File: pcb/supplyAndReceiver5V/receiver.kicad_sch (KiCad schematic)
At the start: 7 parts, among them J1 Conn_01x05_Socket, J1 WAGO 2061-602, J2 har-flexicon 2,54 MSH-4, J4 Kyocera-009176002001906, U2 ISL3280ExHZ

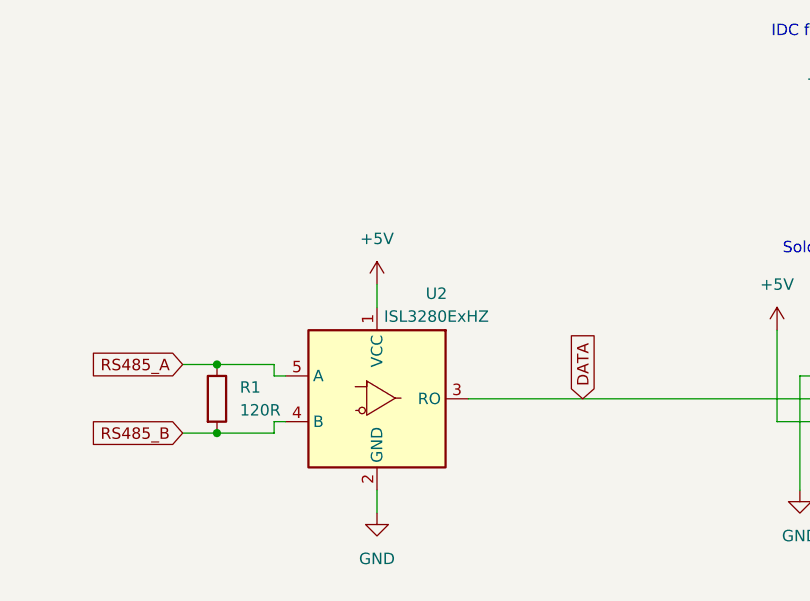
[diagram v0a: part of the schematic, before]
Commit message: Use ISL3280E
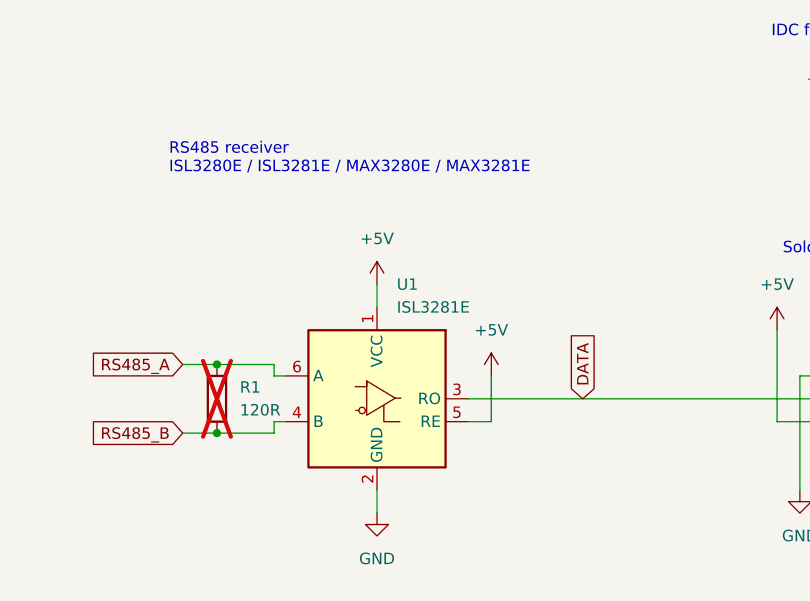
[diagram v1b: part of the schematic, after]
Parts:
- removed U2: ISL3280ExHZ, local:ISL3280E, symbol Interface_UART:ISL3280ExHZ
- added U1: ISL3281E, local:ISL3281E, symbol Interface_UART:ISL3281ExHZ
- R1: now not fitted
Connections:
- net +5V: now also U1.1 (VCC), U1.5 (RE)
- net DATA: now also U1.3 (RO)
- net GND: now also U1.2 (GND)
- net RS485_A: now also U1.6 (A)
- net RS485_B: now also U1.4 (B)
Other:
- note added: "RS485 receiver ISL3280E / ISL3281E / MAX3280E / MAX3281E"
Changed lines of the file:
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@@
+	(wire
+		(pts
+			(xy 135.89 95.25) (xy 135.89 90.17)
+		)
+		(stroke
+			(width 0)
+			(type default)
+		)
+	)
 	(wire
 		(pts
@@
 		(pts
 			(xy 46.99 118.745) (xy 61.595 118.745)
+		)
+		(stroke
+			(width 0)
+			(type default)
+		)
+	)
+	(wire
+		(pts
+			(xy 133.35 95.25) (xy 135.89 95.25)
 		)
 		(stroke
@@
 		)
 	)
+	(text "RS485 receiver\nISL3280E / ISL3281E / MAX3280E / MAX3281E"
+		(exclude_from_sim no)
+		(at 100.076 67.818 0)
+		(effects
+			(font
+				(size 1.27 1.27)
+			)
+			(justify left bottom)
+		)
+	)
 	(text "Solder to LED strip"
 		(exclude_from_sim no)
@@
 	)
 	(symbol
-		(lib_id "Interface_UART:ISL3280ExHZ")
-		(at 123.19 92.71 0)
-		(unit 1)
-		(exclude_from_sim no)
-		(in_bom yes)
-		(on_board yes)
-		(dnp no)
-		(property "Reference" "U2"
-			(at 129.794 81.026 0)
-			(effects
-				(font
-					(size 1.27 1.27)
-				)
-			)
-		)
-		(property "Value" "ISL3280ExHZ"
-			(at 129.794 83.566 0)
-			(effects
-				(font
-					(size 1.27 1.27)
-				)
-			)
-		)
-		(property "Footprint" "local:ISL3280E"
-			(at 125.73 78.74 0)
-			(effects
-				(font
-					(size 1.27 1.27)
-				)
-				(justify left)
-				(hide yes)
-			)
-		)
-		(property "Datasheet" "https://www.renesas.com/us/en/www/doc/datasheet/isl3280e-81e-82e-83e-84e-85e.pdf"
-			(at 100.33 74.93 0)
-			(effects
-				(font
-					(size 1.27 1.27)
-				)
-				(hide yes)
-			)
-		)
-		(property "Description" "RS485, RS422, 20Mbps Transceiver, 3.0V to 5.5V, SOT-23-5"
-			(at 123.19 92.71 0)
-			(effects
-				(font
-					(size 1.27 1.27)
-				)
-				(hide yes)
-			)
-		)
-		(pin "4"
-		)
-		(pin "1"
-		)
-		(pin "2"
-		)
-		(pin "3"
-		)
-		(pin "5"
-		)
-		(instances
-			(project "receiver"
-				(path "/b9a04c3c-65eb-4e1c-b3ab-7b6c9af3c411"
-					(reference "U2")
-					(unit 1)
-				)
-			)
-		)
-	)
-	(symbol
 		(lib_id "power:+15V")
 		(at 61.595 118.745 0)
@@
 	)
 	(symbol
+		(lib_id "power:+5V")
+		(at 135.89 90.17 0)
+		(unit 1)
+		(exclude_from_sim no)
+		(in_bom yes)
+		(on_board yes)
+		(dnp no)
+		(fields_autoplaced yes)
+		(property "Reference" "#PWR08"
+			(at 135.89 93.98 0)
+			(effects
+				(font
+					(size 1.27 1.27)
+				)
+				(hide yes)
+			)
+		)
+		(property "Value" "+5V"
+			(at 135.89 85.09 0)
+			(effects
+				(font
+					(size 1.27 1.27)
+				)
+			)
+		)
+		(property "Footprint" ""
+			(at 135.89 90.17 0)
+			(effects
+				(font
+					(size 1.27 1.27)
+				)
+				(hide yes)
+			)
+		)
+		(property "Datasheet" ""
+			(at 135.89 90.17 0)
+			(effects
+				(font
+					(size 1.27 1.27)
+				)
+				(hide yes)
+			)
+		)
+		(property "Description" ""
+			(at 135.89 90.17 0)
+			(effects
+				(font
+					(size 1.27 1.27)
+				)
+				(hide yes)
+			)
+		)
+		(pin "1"
+		)
+		(instances
+			(project "receiver"
+				(path "/b9a04c3c-65eb-4e1c-b3ab-7b6c9af3c411"
+					(reference "#PWR08")
+					(unit 1)
+				)
+			)
+		)
+	)
+	(symbol
 		(lib_id "power:GND")
 		(at 170.18 102.87 0)
@@
 		(in_bom yes)
 		(on_board yes)
-		(dnp no)
+		(dnp yes)
 		(fields_autoplaced yes)
 		(property "Reference" "R1"
@@
 					(unit 1)
 				)
+			)
+		)
+	)
+	(symbol
+		(lib_id "Interface_UART:ISL3281ExHZ")
+		(at 123.19 92.71 0)
+		(unit 1)
+		(exclude_from_sim no)
+		(in_bom yes)
+		(on_board yes)
+		(dnp no)
+		(fields_autoplaced yes)
+		(property "Reference" "U1"
+			(at 125.3841 80.01 0)
+			(effects
+				(font
+					(size 1.27 1.27)
+				)
+				(justify left)
+			)
+		)
+		(property "Value" "ISL3281E"
+			(at 125.3841 82.55 0)
+			(effects
+				(font
+					(size 1.27 1.27)
+				)
+				(justify left)
+			)
+		)
+		(property "Footprint" "local:ISL3281E"
+			(at 125.73 78.74 0)
+			(effects
+				(font
+					(size 1.27 1.27)
+				)
+				(justify left)
+				(hide yes)
+			)
+		)
+		(property "Datasheet" "https://www.renesas.com/us/en/www/doc/datasheet/isl3280e-81e-82e-83e-84e-85e.pdf"
+			(at 123.19 92.71 0)
+			(effects
+				(font
+					(size 1.27 1.27)
+				)
+				(hide yes)
+			)
+		)
+		(property "Description" "RS485, RS422, 20Mbps Transceiver, 3.0V to 5.5V, SOT-23-6"
+			(at 123.19 92.71 0)
+			(effects
+				(font
+					(size 1.27 1.27)
+				)
+				(hide yes)
+			)
+		)
+		(pin "3"
+		)
+		(pin "5"
+		)
+		(pin "1"
+		)
+		(pin "4"
+		)
+		(pin "6"
+		)
+		(pin "2"
+		)
+		(instances
+			(project "receiver"
+				(path "/b9a04c3c-65eb-4e1c-b3ab-7b6c9af3c411"
+					(reference "U1")
+					(unit 1)
+				)
